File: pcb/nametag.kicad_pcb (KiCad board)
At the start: 2 copper layers, 92 x 57 mm, 36 parts, among them J1 Conn_01x04, SW1 TS-1088-AR02016, U2 BL8536CB3TR36, U3 STC8H1K08-QFN20

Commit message: Update footprints from LCSC EasyEDA Library
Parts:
- BT1: value C5290189 -> BH-AAA-A1AJ001; footprint Battery:BatteryHolder_Keystone_2466_1xAAA -> EasyEDA:BAT-TH_BH-AAA-A1AJ001
- C2: footprint Capacitor_SMD:C_0603_1608Metric_Pad1.08x0.95mm_HandSolder -> Capacitor_SMD:C_0402_1005Metric
- L1: footprint Inductor_SMD:L_Wuerth_PMFI-201610_PMCI-compatible -> EasyEDA:L0806
- SW1: footprint Button_Switch_SMD:SW_Push_SPST_NO_Alps_SKRK -> EasyEDA:SW-SMD_L3.9-W3.0-P4.45
- U2: footprint Package_TO_SOT_SMD:SOT-23 -> EasyEDA:SOT-23-3_L2.9-W1.6-P1.90-LS2.8-BR
- U3: footprint Package_DFN_QFN:QFN-20-1EP_3x3mm_P0.4mm_EP1.65x1.65mm -> EasyEDA:QFN-20_L3.0-W3.0-P0.40-BL-EP1.7
- moved BT1 22.5 mm to (74.2, 87.0), turned to 180 degrees
- moved R8 8.99 mm to (89.2, 86.7)
- moved R6 5.96 mm to (87.6, 86.7)
- moved R1 5.66 mm to (81.8, 84.3)
- moved R3 5.66 mm to (83.8, 84.3)
- moved HO2 4.00 mm to (31.0, 92.0)
- moved HO3 1.80 mm to (117.0, 41.0)
- moved C2 1.71 mm to (81.5, 87.6)
- turned U2 to 90 degrees
- turned U3 to 180 degrees
- renumbered REF** to HO1, REF** to HO2, REF** to HO3
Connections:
- BT1 pad 1: Net-(BT1-+) -> GND
- BT1 pad 2: GND -> Net-(BT1-+)
- R6 pad 1: /Mcu/pwm2 -> /Mcu/pwm4
- R8 pad 1: /Mcu/pwm4 -> /Mcu/pwm2
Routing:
- net /Mcu/cathode0: track 31.9 -> 40.4 mm
- net /Mcu/pwm6: track 9.02 -> 3.97 mm
- net /Mcu/pwm5: track 8.20 -> 3.80 mm
- net /Mcu/pwm2: track 7.15 -> 5.29 mm
- net /Mcu/cathode1: track 54.1 -> 55.7 mm
- net Net-(D9-A): track 44.9 -> 43.4 mm
- net Net-(D1-A): track 43.1 -> 41.6 mm
- net GND: track 15.5 -> 16.5 mm
- net /Mcu/pwm4: track 5.45 -> 4.38 mm
- net Net-(D14-A): track 4.99 -> 4.32 mm
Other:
- board text removed: "Gea"

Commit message: Redo some of the layout, move button
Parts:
- added TP1: TestPoint, TestPoint:TestPoint_Pad_D1.0mm, B.Cu at (51.5, 83.3)
- added TP2: TestPoint, TestPoint:TestPoint_Pad_D1.0mm, B.Cu at (97.0, 83.6)
- added TP3: TestPoint, TestPoint:TestPoint_Pad_D1.0mm, B.Cu at (105.9, 87.8)
- added TP4: TestPoint, TestPoint:TestPoint_Pad_D1.0mm, B.Cu at (108.4, 87.8)
- moved SW1 43.8 mm to (113.0, 87.2), turned to 0 degrees
- moved R2 5.33 mm to (100.2, 90.3)
- moved R4 4.55 mm to (92.4, 88.7)
- moved R7 4.55 mm to (92.4, 90.3)
- moved R5 4.49 mm to (100.2, 88.7)
- moved J1 0.72 mm to (113.5, 91.1)
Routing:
- net /Mcu/switch: track 14.8 -> 32.5 mm, vias 2 -> 0
- net /Mcu/pwm7: track 26.7 -> 18.2 mm
- net Net-(D5-A): track 49.6 -> 54.7 mm
- net /Mcu/pwm8: track 22.8 -> 18.1 mm
- net /Mcu/pwm1: track 11.0 -> 6.67 mm
- net /Mcu/pwm3: track 11.3 -> 7.17 mm
- net /Mcu/UART_TX: track 27.3 -> 31.2 mm
- net /Mcu/UART_RX: track 31.5 -> 35.2 mm
- net Net-(BT1-+): track 23.1 -> 26.8 mm
- net Net-(D13-A): track 10.7 -> 14.0 mm
- net Net-(D10-A): track 4.65 -> 7.82 mm
- net Net-(D11-A): track 30.9 -> 33.5 mm
- net GND: track 16.5 -> 15.9 mm
- net /Mcu/cathode1: track 55.7 -> 55.2 mm
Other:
- board text added: "+"
- board text added: "Aiboo Nametag PCB v2.0 ©xchgeaxeax 2026"
- board text added: "Serial:"
- board text removed: "© xchgeaxeax 2026"

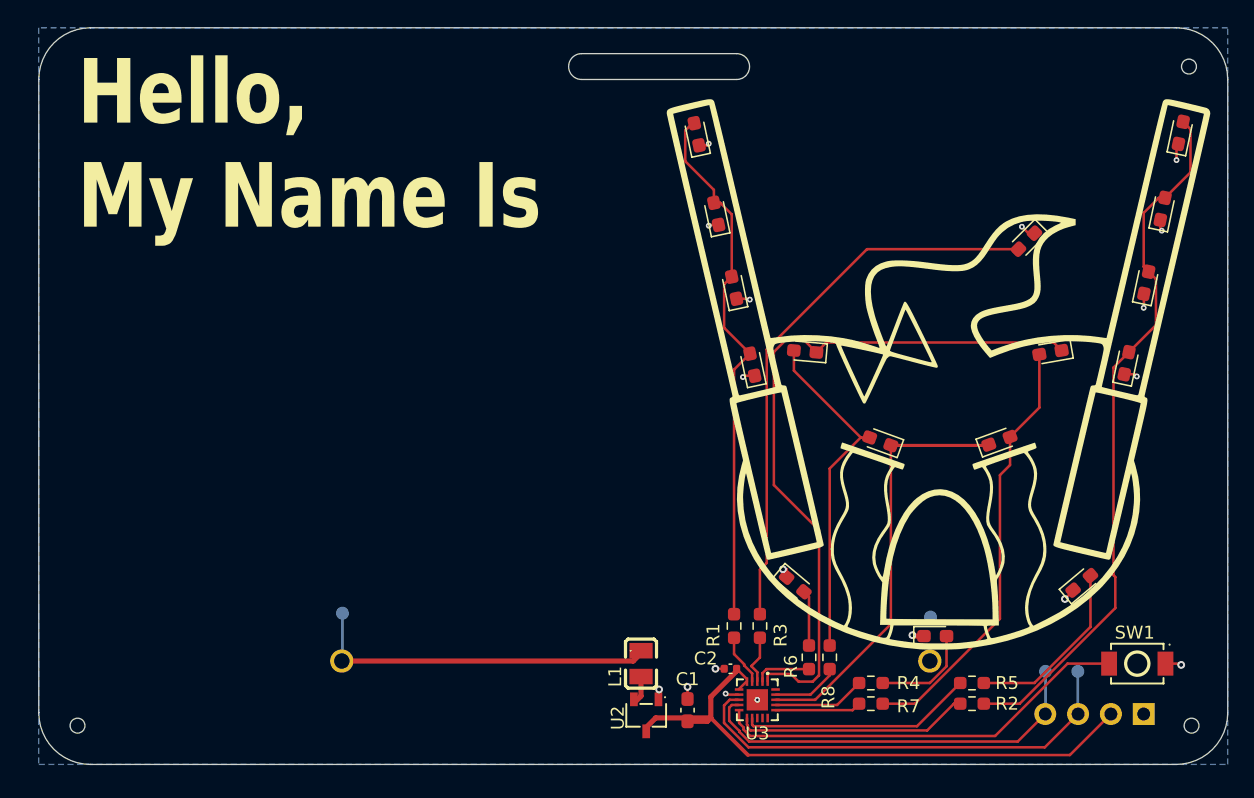
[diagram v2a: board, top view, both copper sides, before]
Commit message: Submit files to JLCPCB for manufacture
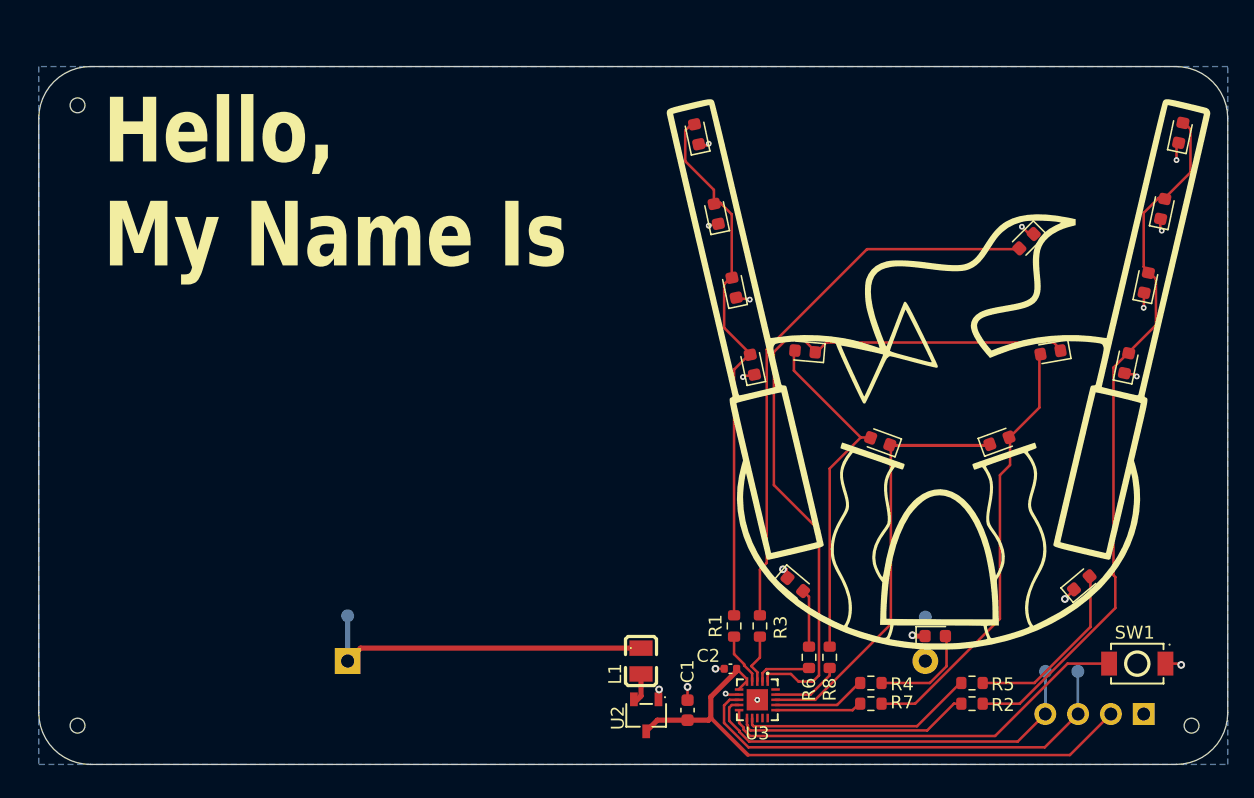
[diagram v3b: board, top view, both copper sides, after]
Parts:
- BT1: value BH-AAA-A1AJ001 -> Battery_Cell; footprint EasyEDA:BAT-TH_BH-AAA-A1AJ001 -> Battery:BatteryHolder_Keystone_2466_1xAAA
- C1: footprint Capacitor_SMD:C_0603_1608Metric_Pad1.08x0.95mm_HandSolder -> Capacitor_SMD:C_0603_1608Metric
- D1, D10, D11, D12, D13, D14, D15, D16, D2, D3, D4, D5, D6, D7, D8, D9: footprint LED_SMD:LED_0603_1608Metric_Pad1.05x0.95mm_HandSolder -> LED_SMD:LED_0603_1608Metric
- R1, R2, R3, R4, R5, R6, R7, R8: footprint Resistor_SMD:R_0603_1608Metric_Pad0.98x0.95mm_HandSolder -> Resistor_SMD:R_0603_1608Metric
- moved HO3 86.1 mm to (31.0, 44.0)
- moved BT1 22.3 mm to (51.9, 87.0), turned to 0 degrees
- moved TP1 0.45 mm to (51.9, 83.5)
- moved TP2 0.40 mm to (96.6, 83.6)
- moved L1 0.20 mm to (74.6, 87.0)
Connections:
- BT1 pad 1: GND -> Net-(BT1-+)
- BT1 pad 2: Net-(BT1-+) -> GND
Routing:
- net +3.3V: track 47.4 -> 45.6 mm
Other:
- board size 92 x 57 mm -> 92 x 54 mm
